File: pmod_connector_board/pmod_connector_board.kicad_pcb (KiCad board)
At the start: 2 copper layers, 120 x 16 mm, 4 parts, among them J1 Conn_02x06_Top_Bottom, J2 Conn_02x06_Top_Bottom, J3 Conn_02x06_Top_Bottom, J4 Conn_02x06_Top_Bottom

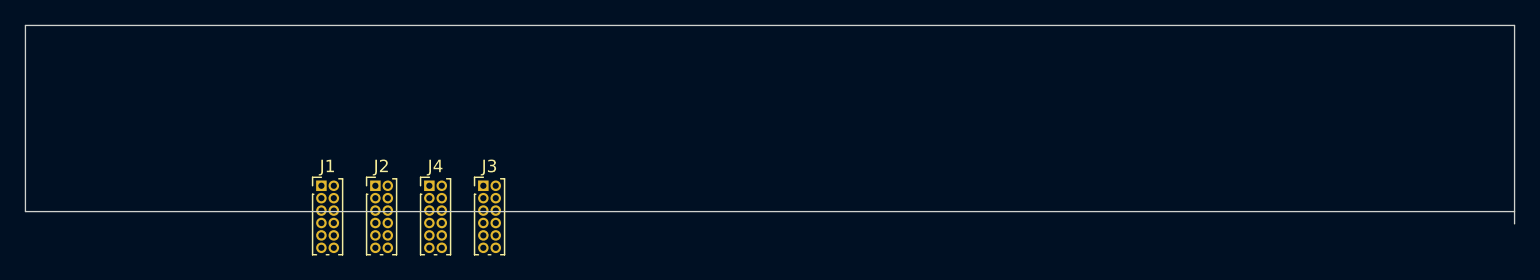
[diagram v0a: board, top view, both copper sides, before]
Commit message: add GND and 3.3V planes
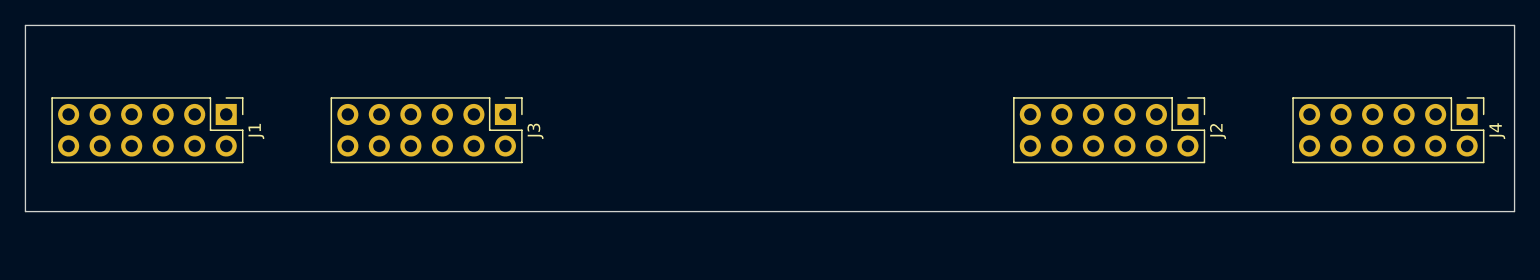
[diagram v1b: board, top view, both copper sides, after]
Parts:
- J1, J2, J3, J4: footprint Connector_PinHeader_1.00mm:PinHeader_2x06_P1.00mm_Vertical -> Connector_PinHeader_2.54mm:PinHeader_2x06_P2.54mm_Vertical
- moved J4 83.8 mm to (136.2, 27.2), turned to -90 degrees
- moved J2 65.7 mm to (113.7, 27.2), turned to -90 degrees
- moved J1 9.58 mm to (36.2, 27.2), turned to -90 degrees
- moved J3 6.01 mm to (58.7, 27.2), turned to -90 degrees
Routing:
- added copper zone on In1.Cu, net +3V3
- added copper zone on In2.Cu, net GND
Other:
- board size 120 x 16 mm -> 120 x 15 mm
- copper layers 2 -> 4
